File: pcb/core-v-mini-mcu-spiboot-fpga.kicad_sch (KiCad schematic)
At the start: 41 parts, among them J1 Conn_02x10_Odd_Even, P1 USB Micro, U1 93C46B, U2 FT4232H-56Q, U3 W25Q, U4 SIT2001BI-S2-33E-12.000000D, Y1 Crystal_GND3

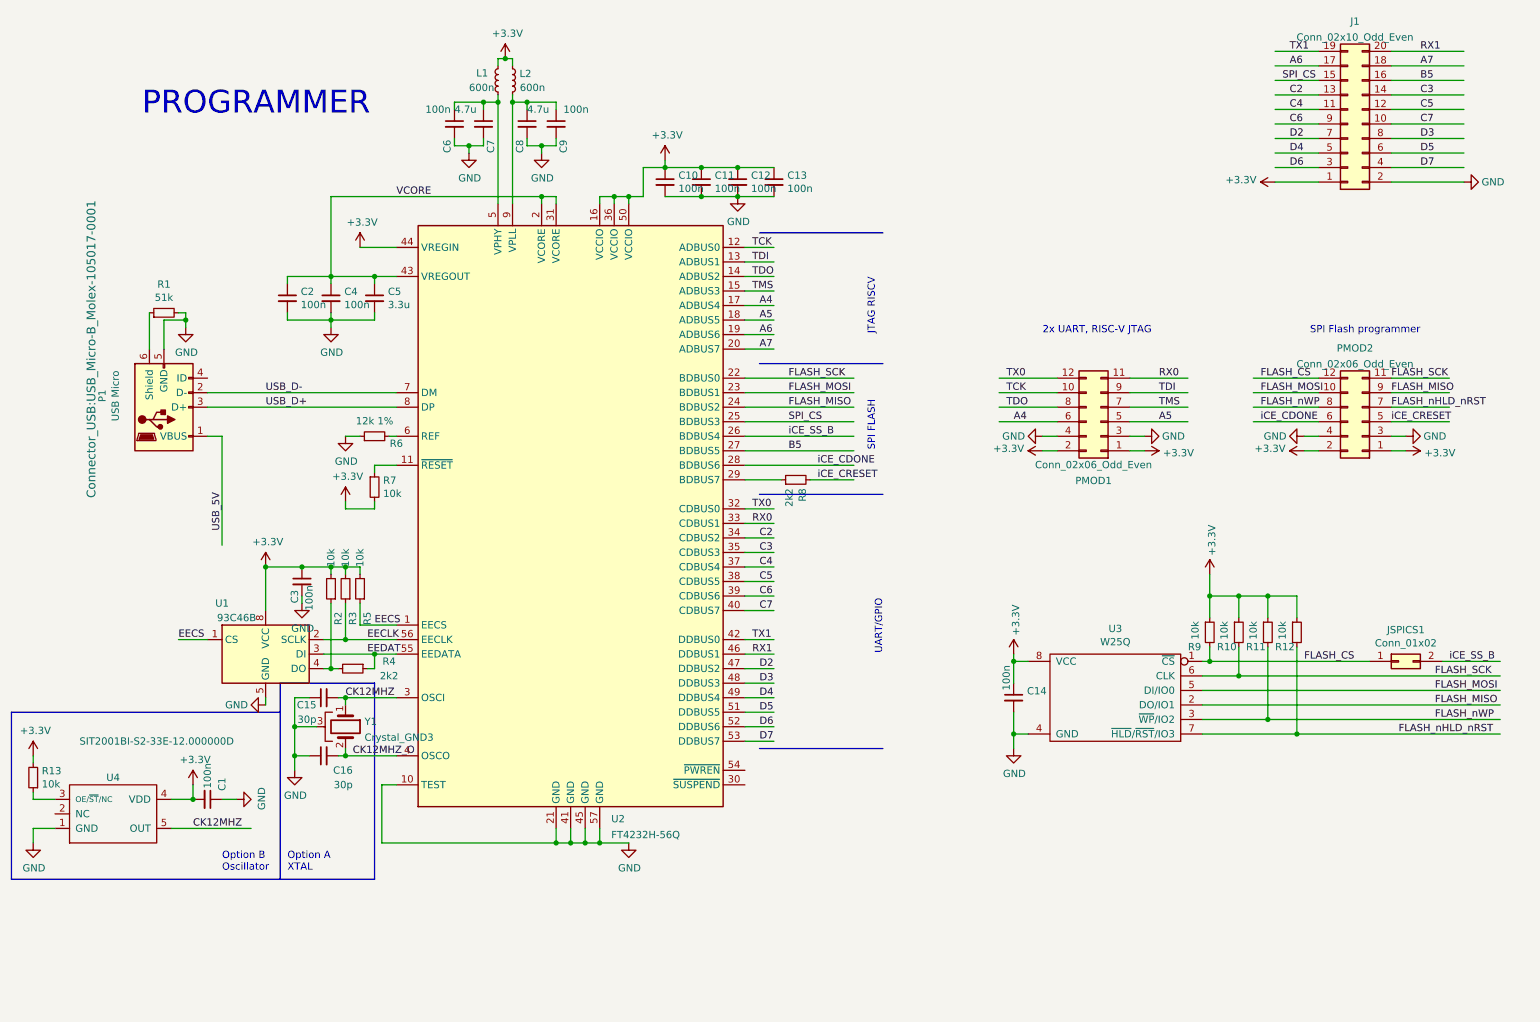
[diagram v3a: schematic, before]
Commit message: Programmer reverted to LQFP package, production files for JLCPCB order added.
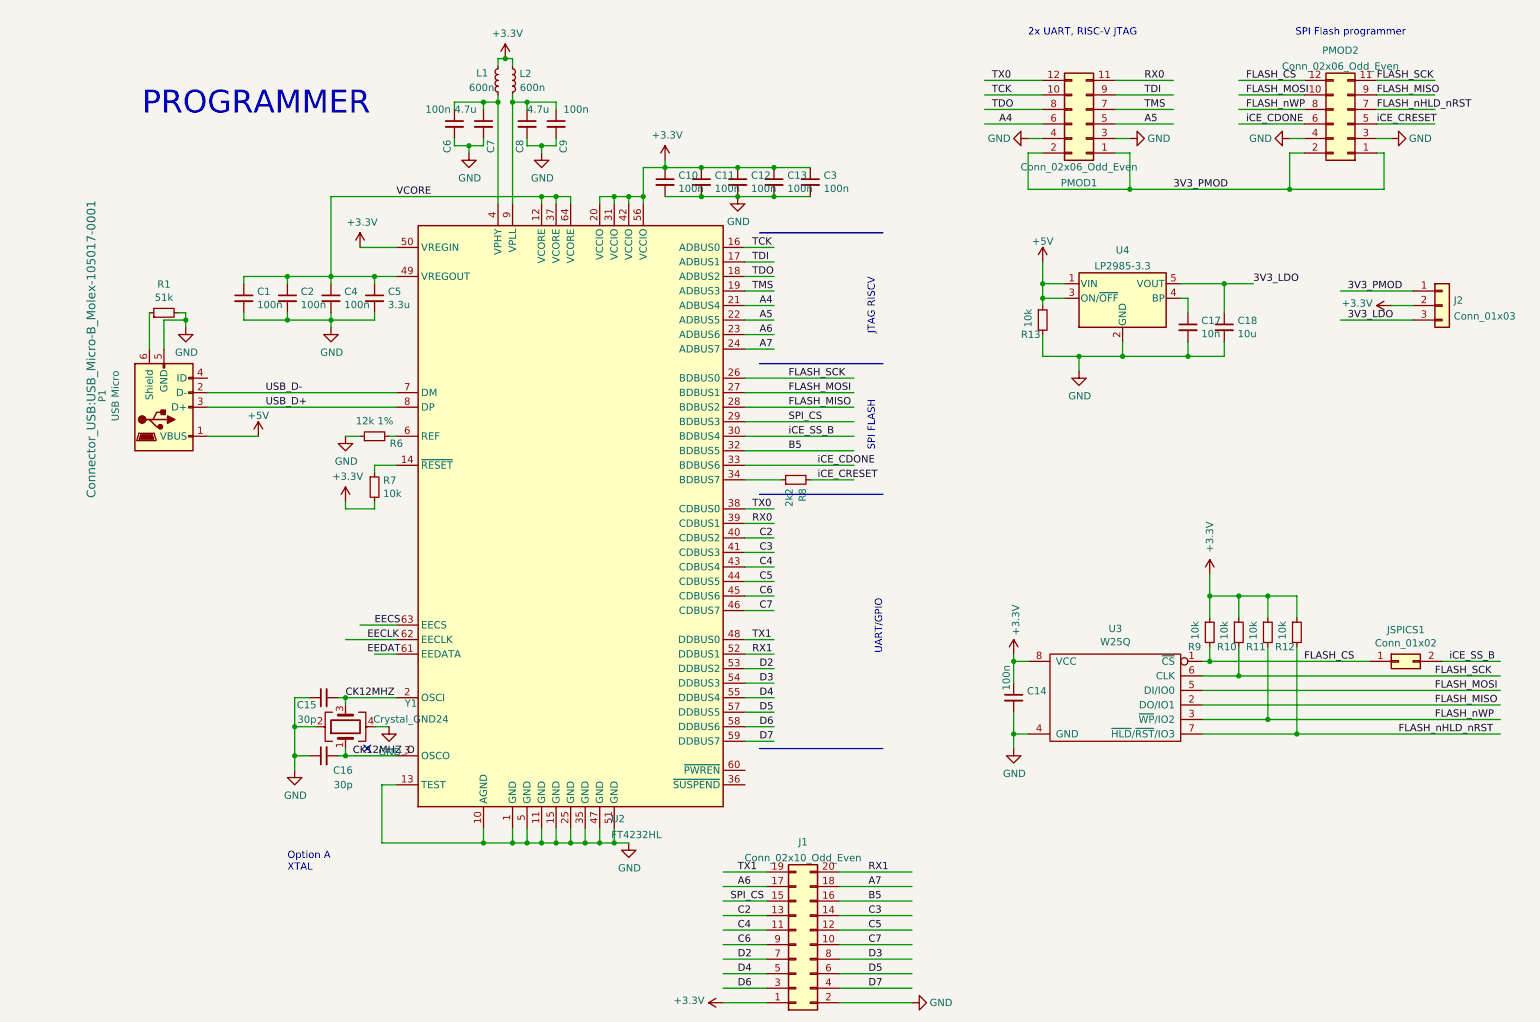
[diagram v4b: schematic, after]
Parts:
- removed R2, R3, R5: 10k, Resistor_SMD:R_0603_1608Metric, symbol Device:R_Small
- removed R4: 2k2, Resistor_SMD:R_0603_1608Metric, symbol Device:R_Small
- removed U1: 93C46B, Package_SO:SSOP-8_3.9x5.05mm_P1.27mm, symbol Memory_EEPROM:93CxxA
- removed U4: SIT2001BI-S2-33E-12.000000D, Package_TO_SOT_SMD:TSOT-23-5_HandSoldering, symbol pkl_device:pkl_oscillator_sit2001
- removed Y1: Crystal_GND3, Crystal:Crystal_DS15_D1.5mm_L5.0mm_Horizontal_1EP_style1, symbol Device:Crystal_GND3
- added C17: 10n, Capacitor_SMD:C_0603_1608Metric, symbol Device:C_Small
- added C18: 10u, Capacitor_SMD:C_0603_1608Metric, symbol Device:C_Small
- added J2: Conn_01x03, Connector_PinHeader_2.54mm:PinHeader_1x03_P2.54mm_Vertical, symbol Connector_Generic:Conn_01x03
- added U4: LP2985-3.3, Package_TO_SOT_SMD:SOT-23-5, symbol Regulator_Linear:LP2985-3.3
- added Y1: Crystal_GND24, Crystal:Crystal_SMD_3225-4Pin_3.2x2.5mm, symbol Device:Crystal_GND24
- U2: value FT4232H-56Q -> FT4232HL; footprint Package_DFN_QFN:QFN-56-1EP_8x8mm_P0.5mm_EP5.9x5.9mm -> Package_QFP:LQFP-64_10x10mm_P0.5mm; symbol core-v-mini-mcu-spiboot-fpga-lib:FT4232H-56Q -> core-v-mini-mcu-spiboot-fpga-lib:FT4232H
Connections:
- net USB_5V is gone; now on net +5V: P1.1 (VBUS)
- net +3V3: now also U2.20 (VCCIO), U2.31 (VCCIO), U2.42 (VCCIO), U2.56 (VCCIO), J2.2 (Pin_2); no longer C1.2, PMOD1.1 (Pin_1), PMOD1.2 (Pin_2), PMOD2.1 (Pin_1), PMOD2.2 (Pin_2), R13.2, U2.16 (VCCIO), U2.36 (VCCIO), U2.44 (VREGIN)
- net A4: now also U2.21 (ADBUS4); no longer U2.17 (ADBUS4)
- net A5: now also U2.22 (ADBUS5); no longer U2.18 (ADBUS5)
- net A6: now also U2.23 (ADBUS6); no longer U2.19 (ADBUS6)
- net A7: now also U2.24 (ADBUS7); no longer U2.20 (ADBUS7)
- net B5: now also U2.32 (BDBUS5); no longer U2.27 (BDBUS5)
- net C2: now also U2.40 (CDBUS2); no longer U2.34 (CDBUS2)
- net C3: now also U2.41 (CDBUS3); no longer U2.35 (CDBUS3)
- net C4: now also U2.43 (CDBUS4); no longer U2.37 (CDBUS4)
- net C5: now also U2.44 (CDBUS5); no longer U2.38 (CDBUS5)
- net C6: now also U2.45 (CDBUS6); no longer U2.39 (CDBUS6)
- net C7: now also U2.46 (CDBUS7); no longer U2.40 (CDBUS7)
- net CK12MHZ: now also U2.2 (OSCI), Y1.3; no longer U2.3 (OSCI)
- net CK12MHZ_O: now also U2.3 (OSCO), Y1.1; no longer U2.4 (OSCO)
- net D2: now also U2.53 (DDBUS2); no longer U2.47 (DDBUS2)
- net D3: now also U2.54 (DDBUS3); no longer U2.48 (DDBUS3)
- net D4: now also U2.55 (DDBUS4); no longer U2.49 (DDBUS4)
- net D5: now also U2.57 (DDBUS5); no longer U2.51 (DDBUS5)
- net D6: now also U2.58 (DDBUS6); no longer U2.52 (DDBUS6)
- net D7: now also U2.59 (DDBUS7); no longer U2.53 (DDBUS7)
- net EECLK: now also U2.62 (EECLK); no longer U2.56 (EECLK)
- net EECS: now also U2.63 (EECS); no longer U2.1 (EECS)
- net EEDAT: no longer U2.55 (EEDATA)
- net FLASH_MISO: now also U2.28 (BDBUS2); no longer U2.24 (BDBUS2)
- net FLASH_MOSI: now also U2.27 (BDBUS1); no longer U2.23 (BDBUS1)
- net FLASH_SCK: now also U2.26 (BDBUS0); no longer U2.22 (BDBUS0)
- net GND: now also C1.2, R13.2, U2.1 (GND), U2.11 (GND), U2.13 (TEST), U2.15 (GND), U2.25 (GND), U2.35 (GND), U2.47 (GND), U2.5 (GND), U2.51 (GND), C17.2, C18.2, U4.2 (GND), Y1.2, Y1.4; no longer C1.1, U2.21 (GND), U2.41 (GND), U2.45 (GND), U2.57 (GND)
- net RX0: now also U2.39 (CDBUS1); no longer U2.33 (CDBUS1)
- net RX1: now also U2.52 (DDBUS1); no longer U2.46 (DDBUS1)
- net SPI_CS: now also U2.29 (BDBUS3); no longer U2.25 (BDBUS3)
- net TCK: now also U2.16 (ADBUS0); no longer U2.12 (ADBUS0)
- net TDI: now also U2.17 (ADBUS1); no longer U2.13 (ADBUS1)
- net TDO: now also U2.18 (ADBUS2); no longer U2.14 (ADBUS2)
- net TMS: now also U2.19 (ADBUS3); no longer U2.15 (ADBUS3)
- net TX0: now also U2.38 (CDBUS0); no longer U2.32 (CDBUS0)
- net TX1: now also U2.48 (DDBUS0); no longer U2.42 (DDBUS0)
- net VCORE: now also C1.1, U2.12 (VCORE), U2.37 (VCORE), U2.49 (VREGOUT), U2.64 (VCORE); no longer U2.2 (VCORE), U2.31 (VCORE), U2.43 (VREGOUT)
- net iCE_CDONE: now also U2.33 (BDBUS6); no longer U2.28 (BDBUS6)
- net iCE_SS_B: now also U2.30 (BDBUS4); no longer U2.26 (BDBUS4)
- net +5V: now reaches R13.1
- net +5V: now also U4.1 (VIN), U4.3 (ON/~{OFF})
- net at C6.1, C7.1, L1.2: now also U2.4 (VPHY); no longer U2.5 (VPHY)
- net at R7.1: now also U2.14 (~{RESET}); no longer U2.11 (~{RESET})
- net at R8.1: now also U2.34 (BDBUS7); no longer U2.29 (BDBUS7)
- new net: C17.1, U4.4 (BP)
- new net 3V3_LDO: C18.1, J2.3 (Pin_3), U4.5 (VOUT)
- new net 3V3_PMOD: J2.1 (Pin_1), PMOD1.1 (Pin_1), PMOD1.2 (Pin_2), PMOD2.1 (Pin_1), PMOD2.2 (Pin_2)
- no-connect marks 0 -> 1
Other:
- note removed: "Option B Oscillator"
- moved on the sheet: J1, PMOD1, PMOD2
